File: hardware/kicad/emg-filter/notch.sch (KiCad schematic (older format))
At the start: 72 parts, among them U20 LM4565, U21 LM4565, U22 LM4565, U23 LM4565, U24 LM4565, U25 LM4565, U26 LM4565, U27 LM4565

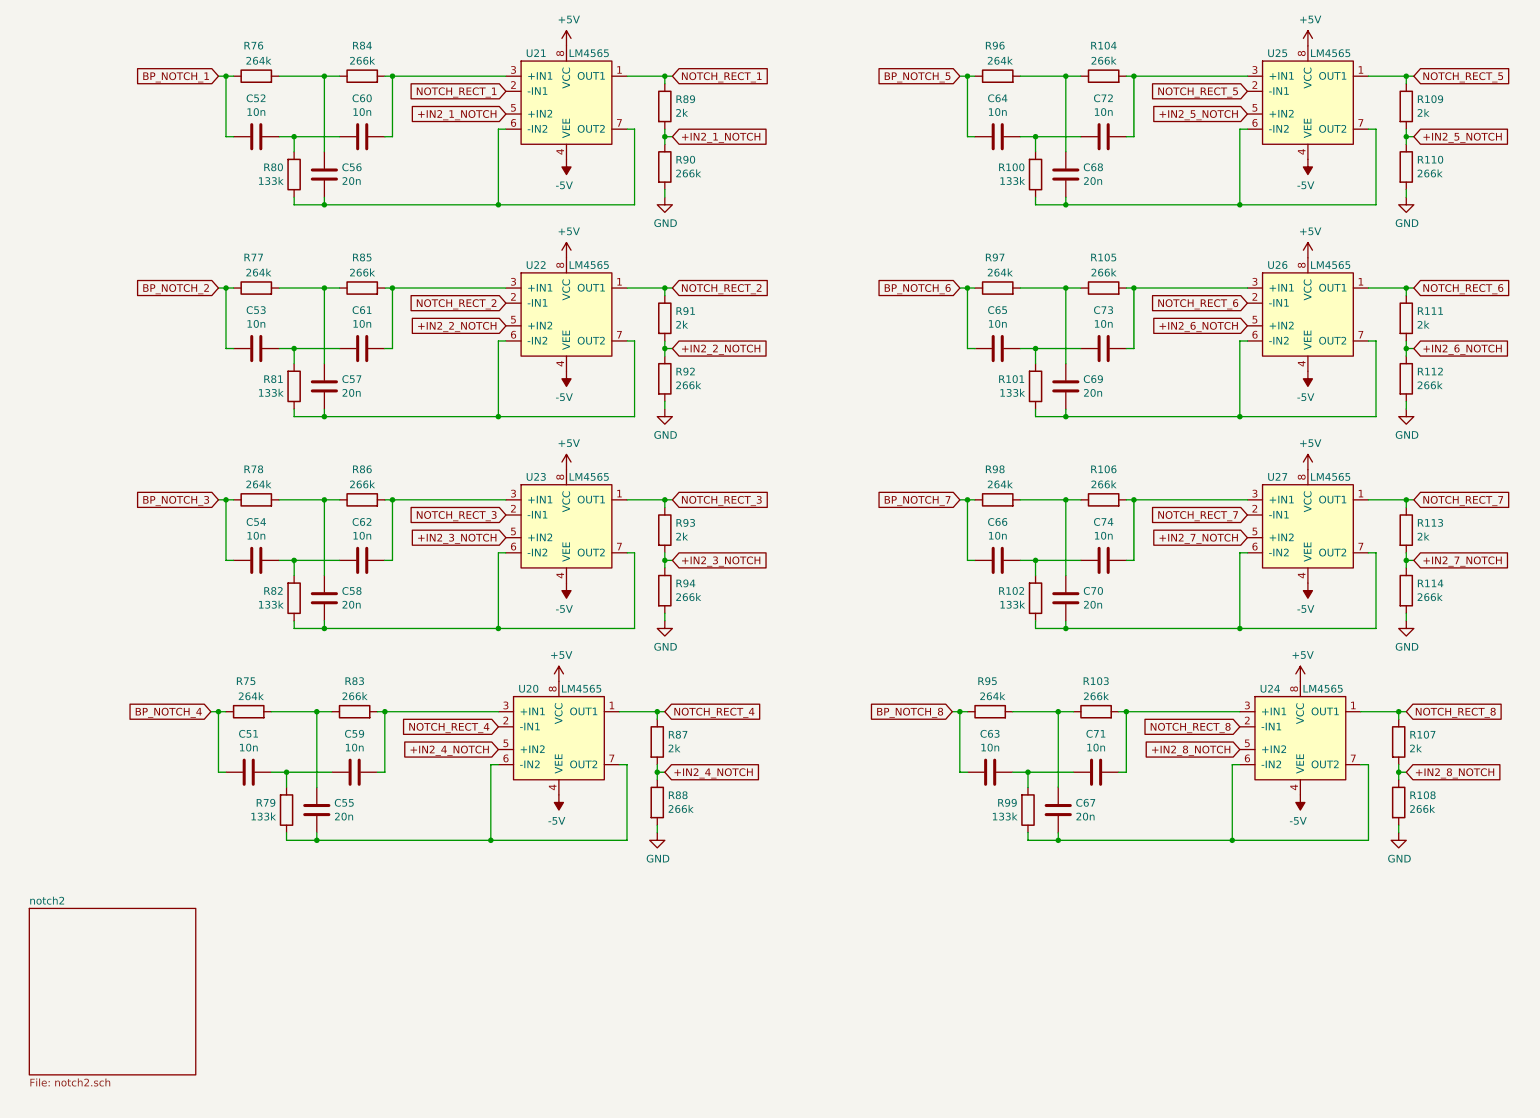
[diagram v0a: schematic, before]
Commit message: pi connector and adc
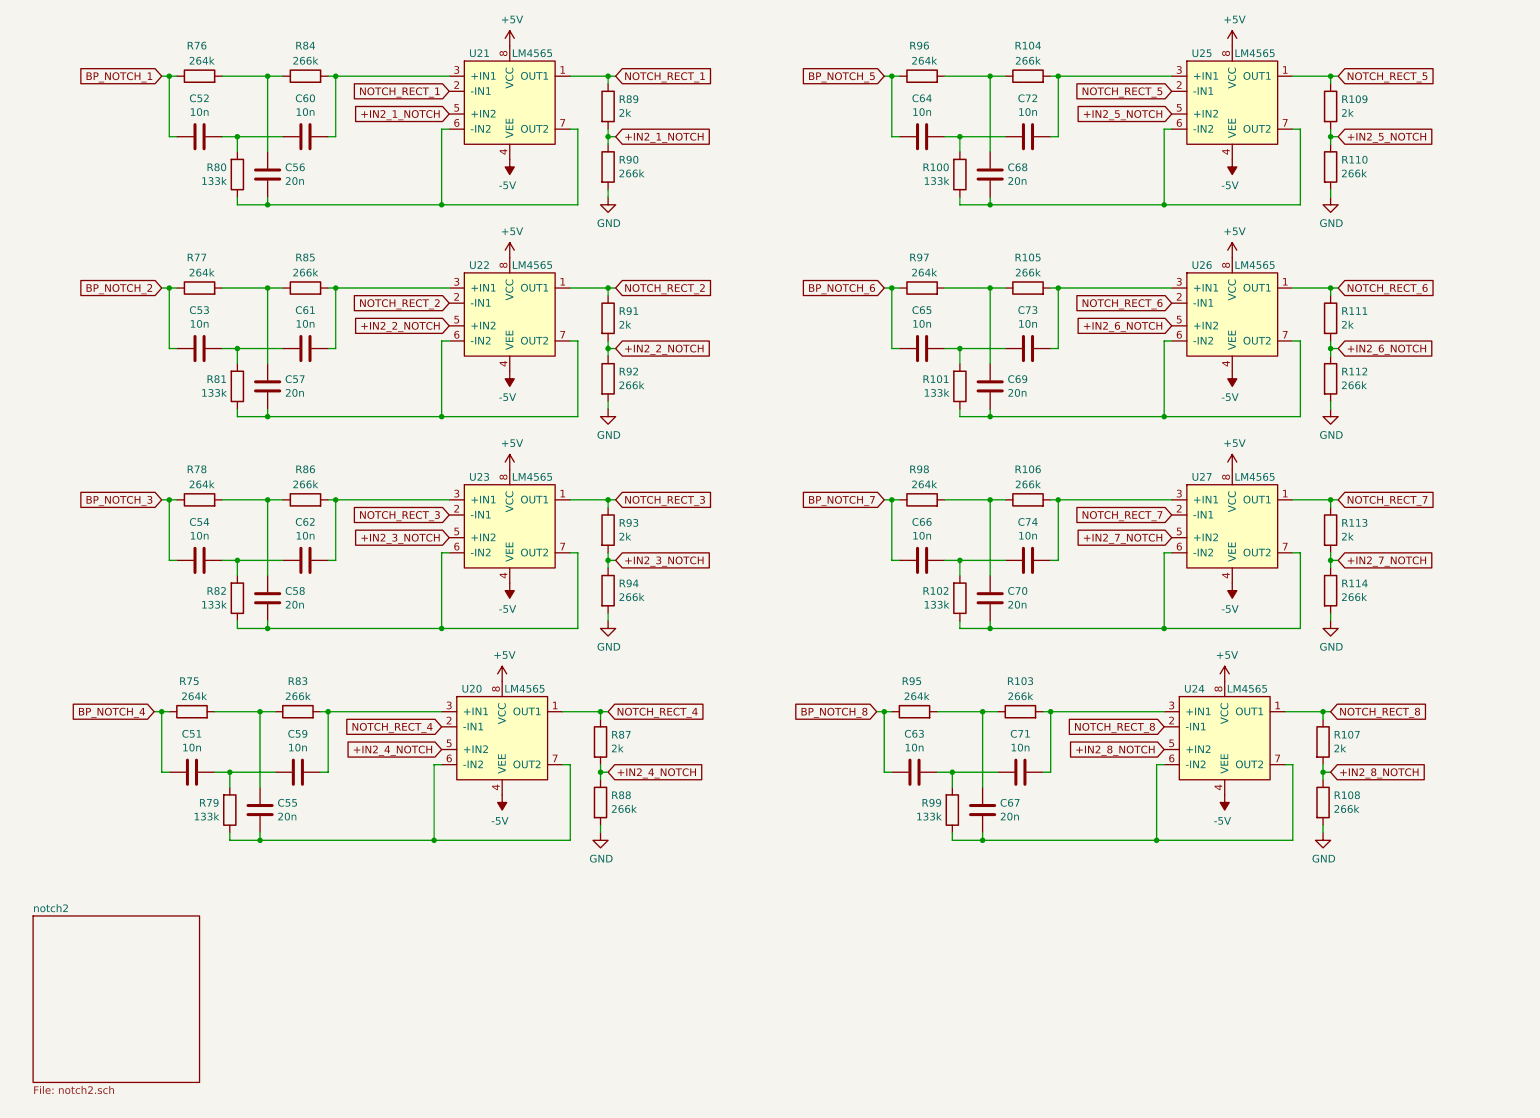
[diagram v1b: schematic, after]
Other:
- moved on the sheet: C51, C52, C53, C54, C55, C56, C57, C58, C59, C60, C61, C62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

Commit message: minor fixes
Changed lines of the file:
@@
 $EndComp
 $Sheet
-S 675  6550 1100 1100
+S 825  6600 1100 1100
 U 61EEB5B0
 F0 "notch2" 50

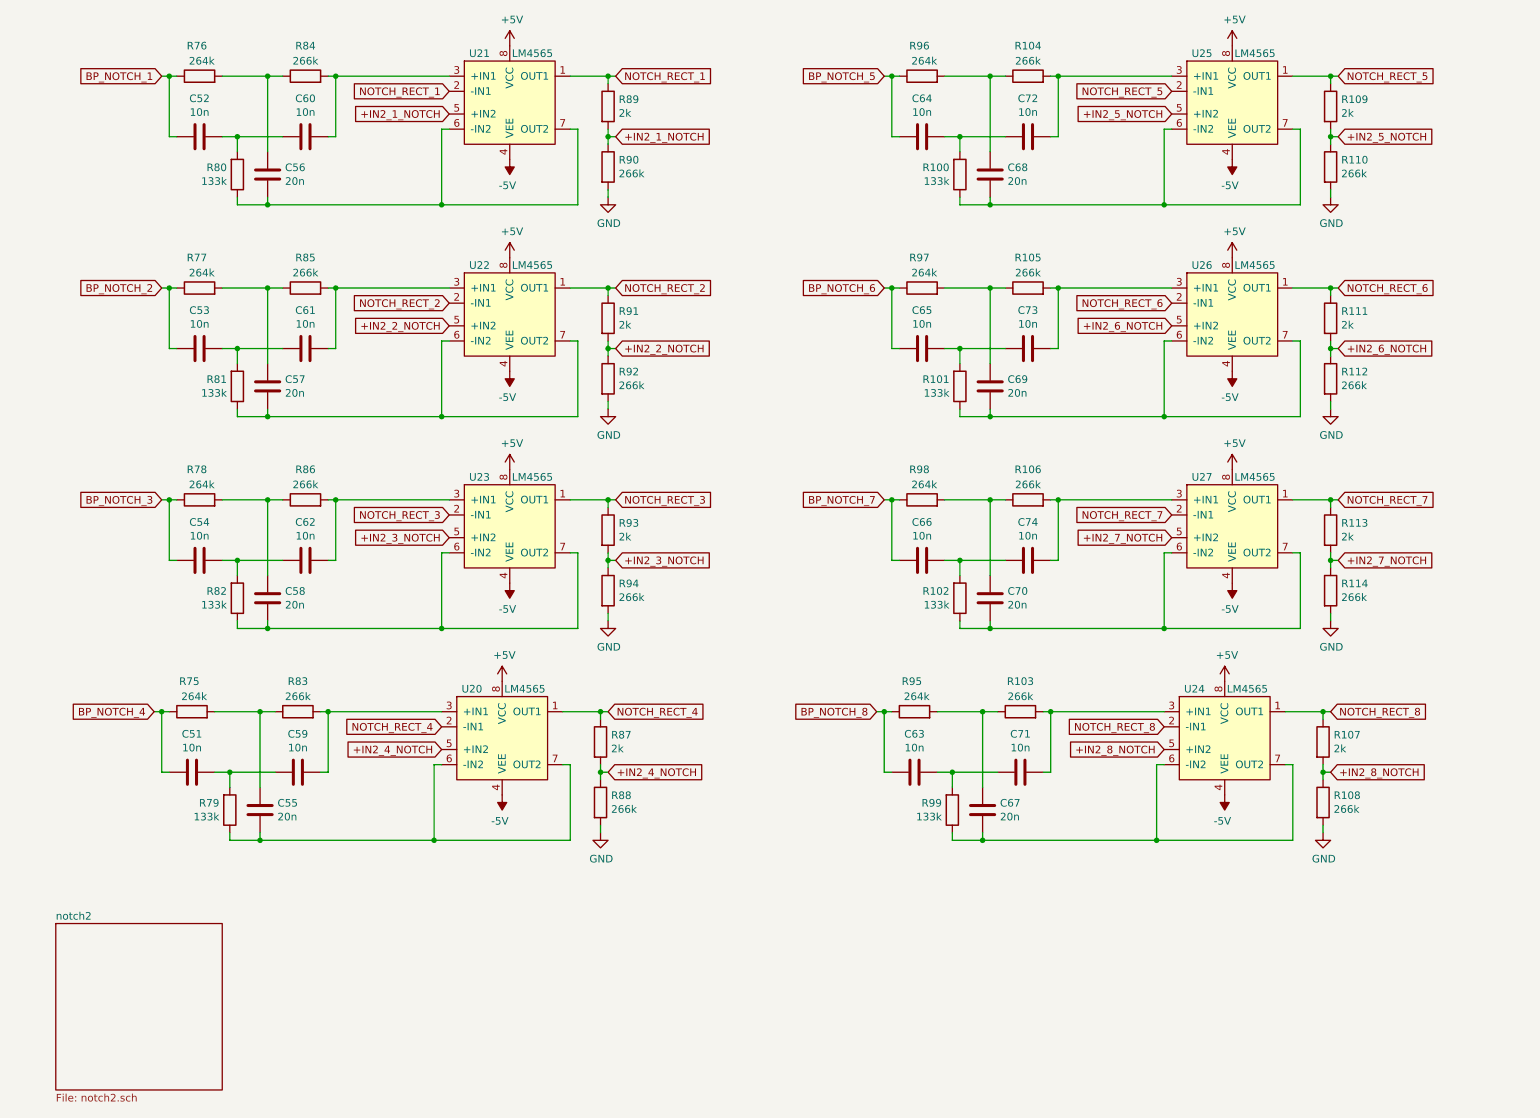
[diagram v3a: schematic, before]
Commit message: fixed rect labels
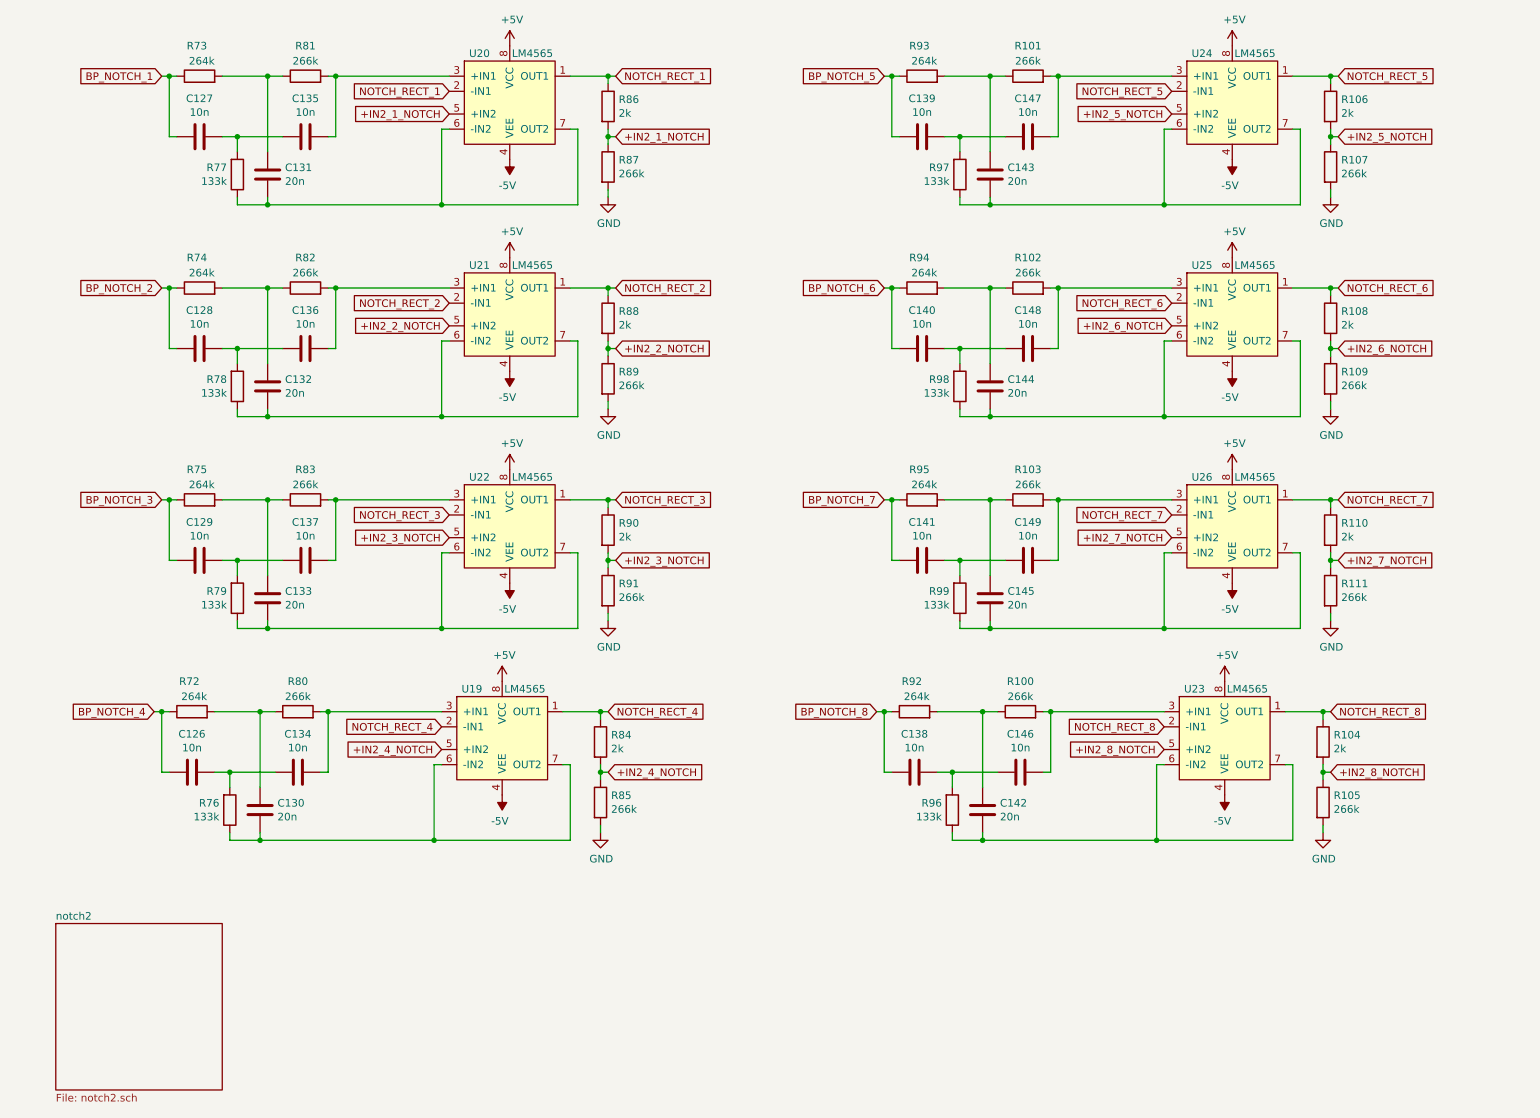
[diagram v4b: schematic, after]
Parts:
- renumbered C51 to C126, C52 to C127, C53 to C128, C54 to C129, C55 to C130, C56 to C131, C57 to C132, C58 to C133, C59 to C134, C60 to C135, C61 to C136, C62 to C137, C63 to C138, C64 to C139, C65 to C140, C66 to C141, C67 to C142, C68 to C143, C69 to C144, C70 to C145, C71 to C146, C72 to C147, C73 to C148, C74 to C149, R103 to R100, R104 to R101, R105 to R102, R106 to R103, R107 to R104, R108 to R105, R109 to R106, R110 to R107, R111 to R108, R112 to R109, R113 to R110, R114 to R111, R75 to R72, R76 to R73, R77 to R74, R78 to R75, R79 to R76, R80 to R77, R81 to R78, R82 to R79, R83 to R80, R84 to R81, R85 to R82, R86 to R83, R87 to R84, R88 to R85, R89 to R86, R90 to R87, R91 to R88, R92 to R89, R93 to R90, R94 to R91, R95 to R92, R96 to R93, R97 to R94, R98 to R95, R99 to R96, R100 to R97, R101 to R98, R102 to R99, U20 to U19, U21 to U20, U22 to U21, U23 to U22, U24 to U23, U25 to U24, U26 to U25, U27 to U26

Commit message: footprint association
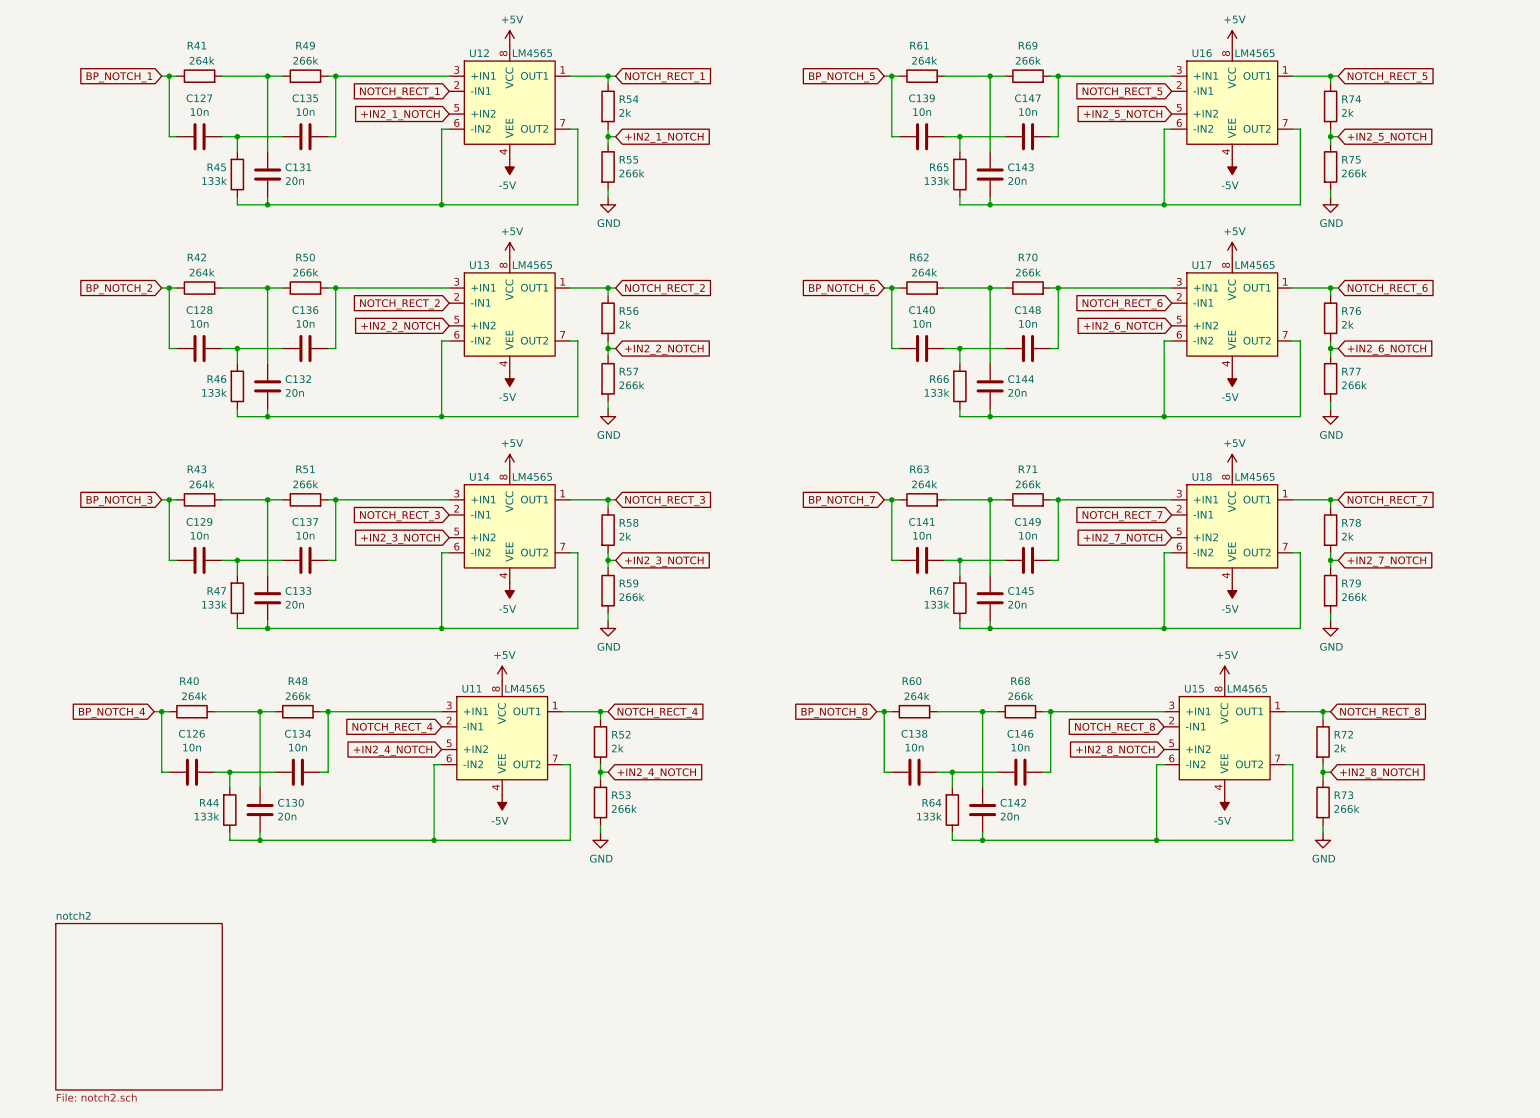
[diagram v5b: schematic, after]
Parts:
- C126, C127, C128, C129, C130, C131, C132, C133, C134, C135, C136, C137, C138, C139, C140, C141, C142, C143, C144, C145, C146, C147, C148, C149: footprint (none) -> Capacitor_SMD:C_0805_2012Metric
- R40: renamed from R72; footprint (none) -> Resistor_SMD:R_0805_2012Metric
- R41: renamed from R73; footprint (none) -> Resistor_SMD:R_0805_2012Metric
- R42: renamed from R74; footprint (none) -> Resistor_SMD:R_0805_2012Metric
- R43: renamed from R75; footprint (none) -> Resistor_SMD:R_0805_2012Metric
- R44: renamed from R76; footprint (none) -> Resistor_SMD:R_0805_2012Metric
- R45: renamed from R77; footprint (none) -> Resistor_SMD:R_0805_2012Metric
- R46: renamed from R78; footprint (none) -> Resistor_SMD:R_0805_2012Metric
- R47: renamed from R79; footprint (none) -> Resistor_SMD:R_0805_2012Metric
- R48: renamed from R80; footprint (none) -> Resistor_SMD:R_0805_2012Metric
- R49: renamed from R81; footprint (none) -> Resistor_SMD:R_0805_2012Metric
- R50: renamed from R82; footprint (none) -> Resistor_SMD:R_0805_2012Metric
- R51: renamed from R83; footprint (none) -> Resistor_SMD:R_0805_2012Metric
- R52: renamed from R84; footprint (none) -> Resistor_SMD:R_0805_2012Metric
- R53: renamed from R85; footprint (none) -> Resistor_SMD:R_0805_2012Metric
- R54: renamed from R86; footprint (none) -> Resistor_SMD:R_0805_2012Metric
- R55: renamed from R87; footprint (none) -> Resistor_SMD:R_0805_2012Metric
- R56: renamed from R88; footprint (none) -> Resistor_SMD:R_0805_2012Metric
- R57: renamed from R89; footprint (none) -> Resistor_SMD:R_0805_2012Metric
- R58: renamed from R90; footprint (none) -> Resistor_SMD:R_0805_2012Metric
- R59: renamed from R91; footprint (none) -> Resistor_SMD:R_0805_2012Metric
- R60: renamed from R92; footprint (none) -> Resistor_SMD:R_0805_2012Metric
- R61: renamed from R93; footprint (none) -> Resistor_SMD:R_0805_2012Metric
- R62: renamed from R94; footprint (none) -> Resistor_SMD:R_0805_2012Metric
- R63: renamed from R95; footprint (none) -> Resistor_SMD:R_0805_2012Metric
- R64: renamed from R96; footprint (none) -> Resistor_SMD:R_0805_2012Metric
- R65: renamed from R97; footprint (none) -> Resistor_SMD:R_0805_2012Metric
- R66: renamed from R98; footprint (none) -> Resistor_SMD:R_0805_2012Metric
- R67: renamed from R99; footprint (none) -> Resistor_SMD:R_0805_2012Metric
- R68: renamed from R100; footprint (none) -> Resistor_SMD:R_0805_2012Metric
- R69: renamed from R101; footprint (none) -> Resistor_SMD:R_0805_2012Metric
- R70: renamed from R102; footprint (none) -> Resistor_SMD:R_0805_2012Metric
- R71: renamed from R103; footprint (none) -> Resistor_SMD:R_0805_2012Metric
- R72: renamed from R104; footprint (none) -> Resistor_SMD:R_0805_2012Metric
- R73: renamed from R105; footprint (none) -> Resistor_SMD:R_0805_2012Metric
- R74: renamed from R106; footprint (none) -> Resistor_SMD:R_0805_2012Metric
- R75: renamed from R107; footprint (none) -> Resistor_SMD:R_0805_2012Metric
- R76: renamed from R108; footprint (none) -> Resistor_SMD:R_0805_2012Metric
- R77: renamed from R109; footprint (none) -> Resistor_SMD:R_0805_2012Metric
- R78: renamed from R110; footprint (none) -> Resistor_SMD:R_0805_2012Metric
- R79: renamed from R111; footprint (none) -> Resistor_SMD:R_0805_2012Metric
- renumbered U19 to U11, U20 to U12, U21 to U13, U22 to U14, U23 to U15, U24 to U16, U25 to U17, U26 to U18
